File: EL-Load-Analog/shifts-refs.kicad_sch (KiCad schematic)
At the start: 37 parts, among them U10 TL072/OPA2376, U16 TPS7A2030, U17 TPS72325, U21 LT1964-5, U22 AMS1117, U23 TLV1117-50, U4 REF5025AD

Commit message: Working on #4,#2 fixed #8,#22
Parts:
- removed R39: 91, Resistor_SMD:R_0805_2012Metric, symbol Device:R_Small
- C29: Part Name C_2.2uF_10V_X7R_10%_0805 -> C_2.2uF_25V_X7R_10%_0805
- R40: value 1k8 -> 200; Part Name R_1.8kΩ_0805_1% -> R_200.0Ω_0805_1%
- R41: value 220 -> 1k8; Part Name R_220.0Ω_0805_1% -> R_1.8kΩ_0805_1%
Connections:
- net +12V: now also R40.1
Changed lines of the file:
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@@
   (junction (at 73.66 57.15) (diameter 0) (color 0 0 0 0)
   )
+  (junction (at 208.915 35.56) (diameter 0) (color 0 0 0 0)
+  )
   (junction (at 35.56 71.755) (diameter 0) (color 0 0 0 0)
   )
@@
   )
   (junction (at 215.265 81.915) (diameter 0) (color 0 0 0 0)
-  )
-  (junction (at 208.915 35.56) (diameter 0) (color 0 0 0 0)
   )
   (junction (at 82.55 43.18) (diameter 0) (color 0 0 0 0)
@@
     (stroke (width 0) (type default))
   )
+  (wire (pts (xy 208.915 35.56) (xy 215.265 35.56))
+    (stroke (width 0) (type default))
+  )
   (polyline (pts (xy 13.97 114.935) (xy 180.34 114.935))
     (stroke (width 0) (type dash))
@@
     (stroke (width 0) (type default))
   )
-  (wire (pts (xy 208.915 40.64) (xy 208.915 41.91))
+  (wire (pts (xy 208.915 35.56) (xy 208.915 41.91))
     (stroke (width 0) (type default))
   )
@@
     (stroke (width 0) (type default))
   )
+  (wire (pts (xy 255.27 70.485) (xy 255.27 67.945))
+    (stroke (width 0) (type default))
+  )
+  (wire (pts (xy 204.47 54.61) (xy 208.915 54.61))
+    (stroke (width 0) (type default))
+  )
+  (wire (pts (xy 64.77 55.88) (xy 64.77 57.15))
+    (stroke (width 0) (type default))
+  )
+  (wire (pts (xy 109.855 132.715) (xy 109.855 133.985))
+    (stroke (width 0) (type default))
+  )
+  (wire (pts (xy 114.3 48.26) (xy 114.3 54.61))
+    (stroke (width 0) (type default))
+  )
+  (wire (pts (xy 64.77 57.15) (xy 73.66 57.15))
+    (stroke (width 0) (type default))
+  )
+  (wire (pts (xy 106.68 179.705) (xy 109.22 179.705))
+    (stroke (width 0) (type default))
+  )
+  (wire (pts (xy 244.475 67.945) (xy 244.475 70.485))
+    (stroke (width 0) (type default))
+  )
   (wire (pts (xy 208.28 35.56) (xy 208.915 35.56))
-    (stroke (width 0) (type default))
-  )
-  (wire (pts (xy 255.27 70.485) (xy 255.27 67.945))
-    (stroke (width 0) (type default))
-  )
-  (wire (pts (xy 204.47 54.61) (xy 208.915 54.61))
-    (stroke (width 0) (type default))
-  )
-  (wire (pts (xy 64.77 55.88) (xy 64.77 57.15))
-    (stroke (width 0) (type default))
-  )
-  (wire (pts (xy 109.855 132.715) (xy 109.855 133.985))
-    (stroke (width 0) (type default))
-  )
-  (wire (pts (xy 114.3 48.26) (xy 114.3 54.61))
-    (stroke (width 0) (type default))
-  )
-  (wire (pts (xy 64.77 57.15) (xy 73.66 57.15))
-    (stroke (width 0) (type default))
-  )
-  (wire (pts (xy 106.68 179.705) (xy 109.22 179.705))
-    (stroke (width 0) (type default))
-  )
-  (wire (pts (xy 244.475 67.945) (xy 244.475 70.485))
-    (stroke (width 0) (type default))
-  )
-  (wire (pts (xy 208.915 35.56) (xy 215.265 35.56))
     (stroke (width 0) (type default))
   )
@@
       (effects (font (size 1.27 1.27)) hide)
     )
-    (property "Part Name" "C_2.2uF_10V_X7R_10%_0805" (at 113.03 165.1 0)
+    (property "Part Name" "C_2.2uF_25V_X7R_10%_0805" (at 113.03 165.1 0)
       (effects (font (size 1.27 1.27)) hide)
     )
@@
       (effects (font (size 1.27 1.27)) (justify left))
     )
-    (property "Value" "220" (at 211.455 52.0699 0)
+    (property "Value" "1k8" (at 211.455 52.0699 0)
       (effects (font (size 1.27 1.27)) (justify left))
     )
@@
       (effects (font (size 1.27 1.27)) hide)
     )
-    (property "Part Name" "R_220.0Ω_0805_1%" (at 208.915 50.8 0)
+    (property "Part Name" "R_1.8kΩ_0805_1%" (at 208.915 50.8 0)
       (effects (font (size 1.27 1.27)) hide)
     )
@@
       (effects (font (size 1.27 1.27)) (justify left))
     )
-    (property "Value" "1k8" (at 210.82 45.72 0)
+    (property "Value" "200" (at 210.82 45.72 0)
       (effects (font (size 1.27 1.27)) (justify left))
     )
@@
       (effects (font (size 1.27 1.27)) hide)
     )
-    (property "Part Name" "R_1.8kΩ_0805_1%" (at 208.915 44.45 0)
+    (property "Part Name" "R_200.0Ω_0805_1%" (at 208.915 44.45 0)
       (effects (font (size 1.27 1.27)) hide)
     )
@@
     )
   )
-  (symbol (lib_id "Device:R_Small") (at 208.915 38.1 0) (unit 1)
-    (in_bom yes) (on_board yes) (dnp no) (fields_autoplaced)
-    (property "Reference" "R39" (at 210.82 36.83 0)
-      (effects (font (size 1.27 1.27)) (justify left))
-    )
-    (property "Value" "91" (at 210.82 39.37 0)
-      (effects (font (size 1.27 1.27)) (justify left))
-    )
-    (property "Footprint" "Resistor_SMD:R_0805_2012Metric" (at 208.915 38.1 0)
-      (effects (font (size 1.27 1.27)) hide)
-    )
-    (property "Datasheet" "~" (at 208.915 38.1 0)
-      (effects (font (size 1.27 1.27)) hide)
-    )
-    (property "Part Name" "R_91.0Ω_0805_1%" (at 208.915 38.1 0)
-      (effects (font (size 1.27 1.27)) hide)
-    )
-    (pin "1")
-    (pin "2")
-    (instances
-      (project "EL-Load-Analog"
-        (path "/51d9228f-95b8-4f0d-bdba-83c3975c517c/73a2922e-6b99-4e2c-8c0a-1f11161a60e3"
-          (reference "R39") (unit 1)
-        )
-      )
-    )
-  )
   (symbol (lib_id "power:-6V") (at 215.265 88.9 180) (unit 1)
     (in_bom yes) (on_board yes) (dnp no) (fields_autoplaced)
@@
       (effects (font (size 1.27 1.27)) hide)
     )
-    (property "Part Name" "C_2.2uF_10V_X7R_10%_0805" (at 79.375 163.83 0)
-      (effects (font (size 1.27 1.27)) hide)
-    )
+    (property "Part Name" "C_2.2uF_25V_X7R_10%_0805" (at 79.375 163.83 0)
+      (effects (font (size 1.27 1.27)) hide)
+    )

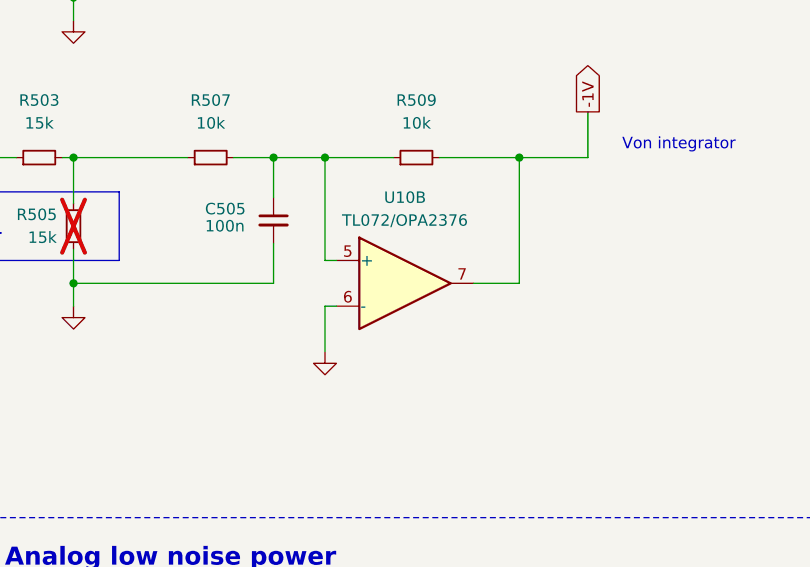
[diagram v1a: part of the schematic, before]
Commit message: Fixing issues from #4, adding ESD protection (#6)
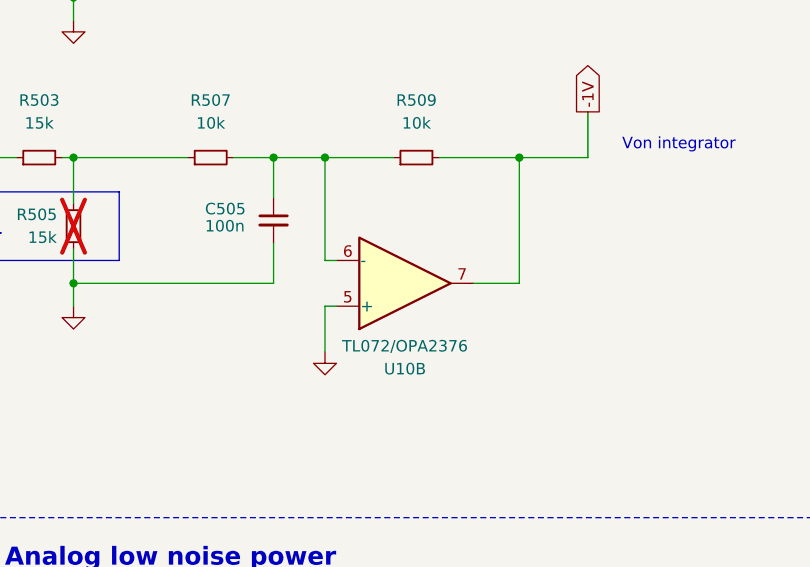
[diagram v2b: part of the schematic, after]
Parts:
- U21: Part Name U_LT1964ES5 -> U_LT1964ES5-5
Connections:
- net GND: now also U10.5 (+); no longer U10.6 (-)
- net at C505.1, R507.2, R509.1: now also U10.6 (-); no longer U10.5 (+)
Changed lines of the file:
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@@
       (effects (font (size 1.27 1.27)) hide)
     )
-    (property "Part Name" "U_LT1964ES5" (at 230.505 79.375 0)
+    (property "Part Name" "U_LT1964ES5-5" (at 230.505 79.375 0)
       (effects (font (size 1.27 1.27)) hide)
     )
@@
     )
   )
-  (symbol (lib_id "Amplifier_Operational:TL072") (at 128.27 88.9 0) (unit 2)
-    (in_bom yes) (on_board yes) (dnp no) (fields_autoplaced)
-    (property "Reference" "U10" (at 128.27 79.375 0)
+  (symbol (lib_id "Amplifier_Operational:TL072") (at 128.27 88.9 0) (mirror x) (unit 2)
+    (in_bom yes) (on_board yes) (dnp no)
+    (property "Reference" "U10" (at 128.27 98.425 0)
       (effects (font (size 1.27 1.27)))
     )
-    (property "Value" "TL072/OPA2376" (at 128.27 81.915 0)
+    (property "Value" "TL072/OPA2376" (at 128.27 95.885 0)
       (effects (font (size 1.27 1.27)))
     )

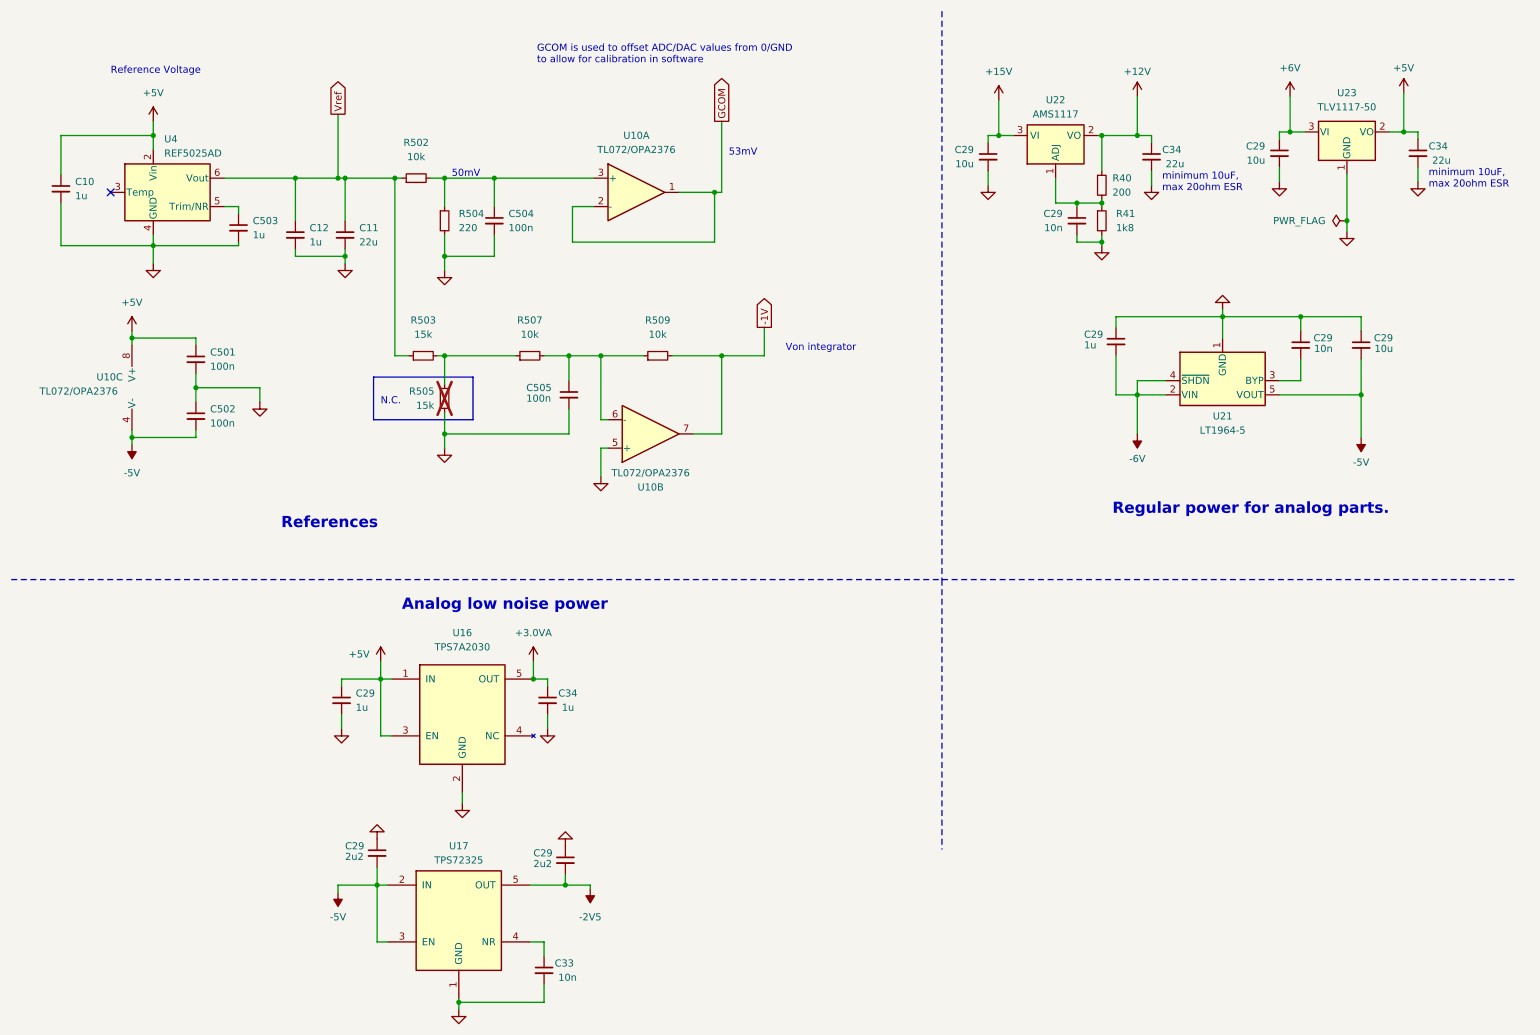
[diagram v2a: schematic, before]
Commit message: Added heatsink moutingholes, reverse polarity, moved snubbers.
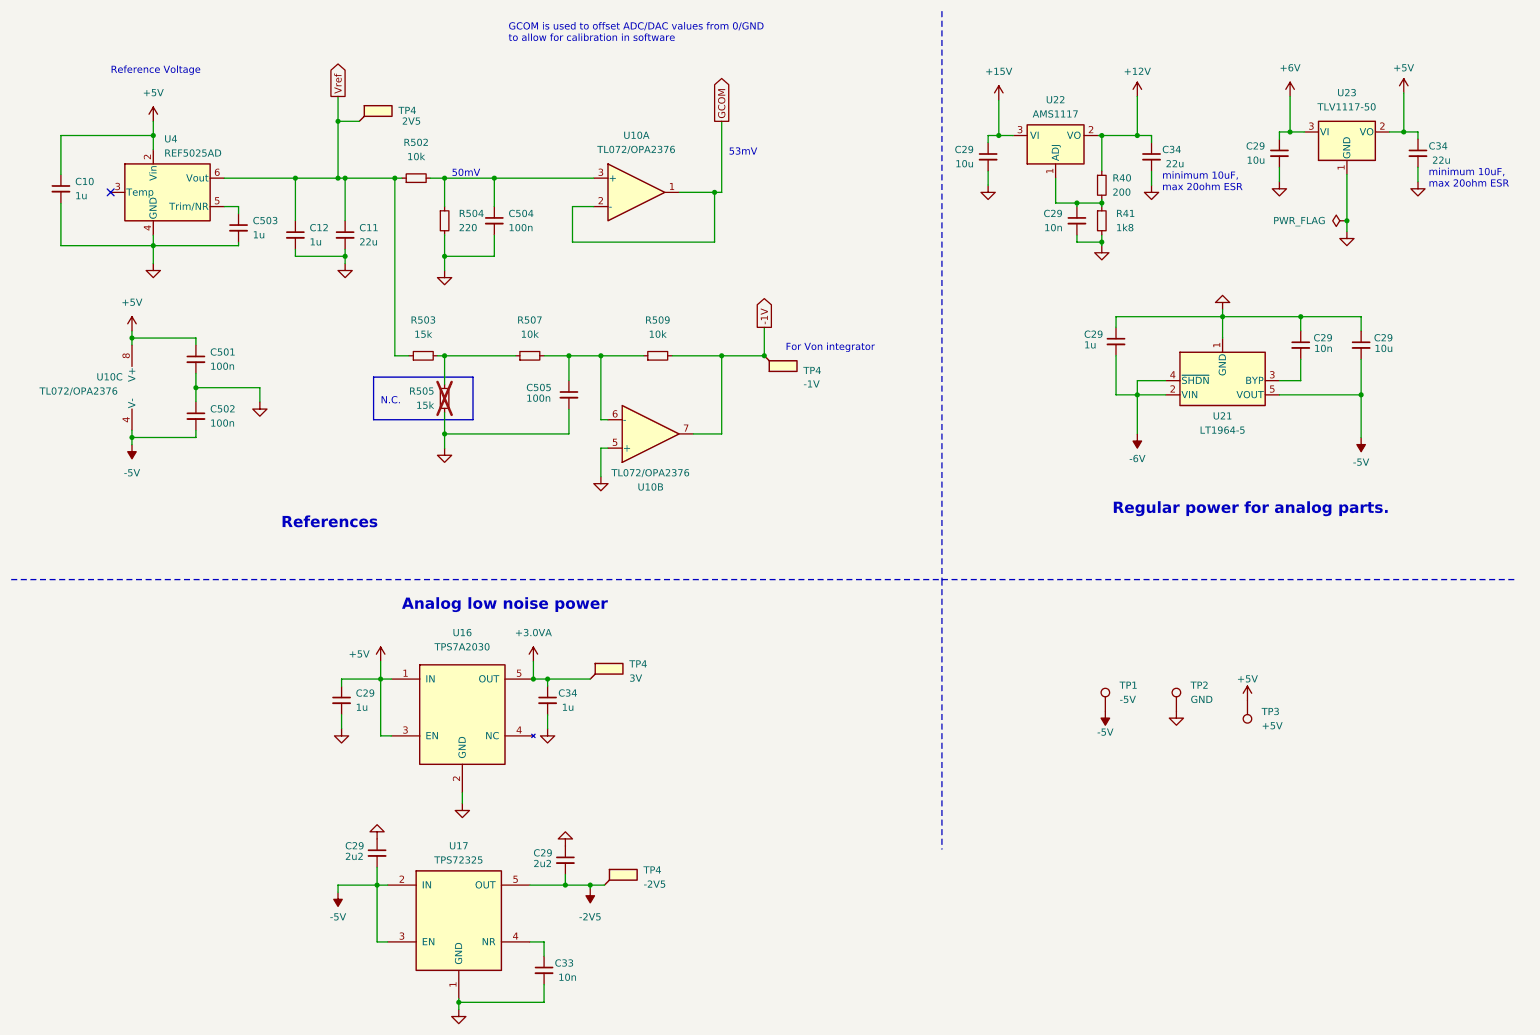
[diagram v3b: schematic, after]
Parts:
- added TP1: -5V, TestPoint:TestPoint_Loop_D1.80mm_Drill1.0mm_Beaded, symbol Connector:TestPoint
- added TP2: GND, TestPoint:TestPoint_Loop_D2.50mm_Drill1.0mm, symbol Connector:TestPoint
- added TP3: +5V, TestPoint:TestPoint_Loop_D1.80mm_Drill1.0mm_Beaded, symbol Connector:TestPoint
- added TP4: 3V, TestPoint:TestPoint_Pad_1.0x1.0mm, symbol Connector:TestPoint_Flag
- added TP4: -2V5, TestPoint:TestPoint_Pad_1.0x1.0mm, symbol Connector:TestPoint_Flag
- added TP4: 2V5, TestPoint:TestPoint_Pad_1.0x1.0mm, symbol Connector:TestPoint_Flag
- added TP4: -1V, TestPoint:TestPoint_Pad_1.0x1.0mm, symbol Connector:TestPoint_Flag
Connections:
- net +3.0VA: now also TP4.1
- net +5V: now also TP3.1
- net -1V: now also TP4.1
- net -2V5: now also TP4.1
- net -5V: now also TP1.1
- net GND: now also TP2.1
- net Vref: now also TP4.1
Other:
- note added: "For Von integrator"
- note removed: "Von integrator"

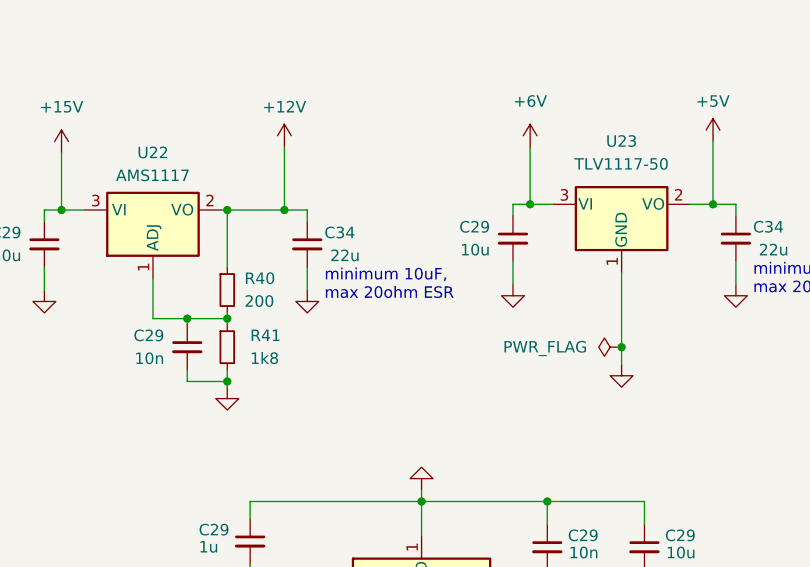
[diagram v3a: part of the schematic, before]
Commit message: v4 Analog board design. Features reverse polarity, remote sense error and new clamping circuitry.
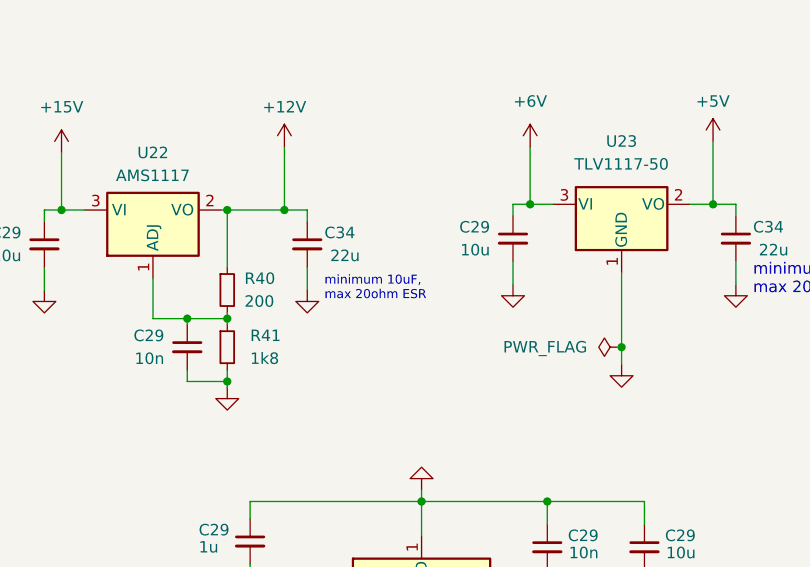
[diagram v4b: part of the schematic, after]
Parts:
- C29: Part Name C_10.0uF_25V_X7R_10%_0805 -> C_10.0uF_25V_X5R_10%_0805
- C501, C502, C504, C505: Part Name C_100.0nF_0805_20% -> C_100.0nF_50V_0805_10%_X7R
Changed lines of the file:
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@@
   (title_block
     (title "Electronic Load Analog Test Board")
-    (date "2024-02-06")
+    (date "2024-11-10")
     (rev "${VERSION}")
     (comment 1 "License: CERN-OHL-W-2.0")
@@
   )
   (text "minimum 10uF, \nmax 20ohm ESR" (at 219.71 45.72 0)
-    (effects (font (size 1.27 1.27)) (justify left bottom))
+    (effects (font (size 1 1)) (justify left bottom))
   )
   (text "GCOM is used to offset ADC/DAC values from 0/GND \nto allow for calibration in software\n"
@@
       (effects (font (size 1.27 1.27)) hide)
     )
-    (property "Part Name" "C_10.0uF_25V_X7R_10%_0805" (at 255.27 73.025 0)
+    (property "Part Name" "C_10.0uF_25V_X5R_10%_0805" (at 255.27 73.025 0)
       (effects (font (size 1.27 1.27)) hide)
     )
@@
       (effects (font (size 1.27 1.27)) hide)
     )
-    (property "Part Name" "C_10.0uF_25V_X7R_10%_0805" (at 240.665 38.735 0)
+    (property "Part Name" "C_10.0uF_25V_X5R_10%_0805" (at 240.665 38.735 0)
       (effects (font (size 1.27 1.27)) hide)
     )
@@
       (effects (font (size 1.27 1.27)) hide)
     )
-    (property "Part Name" "C_100.0nF_0805_20%" (at 46.99 75.565 0)
+    (property "Part Name" "C_100.0nF_50V_0805_10%_X7R " (at 46.99 75.565 0)
       (effects (font (size 1.27 1.27)) hide)
     )
@@
       (effects (font (size 1.27 1.27)) hide)
     )
-    (property "Part Name" "C_10.0uF_25V_X7R_10%_0805" (at 188.595 39.37 0)
+    (property "Part Name" "C_10.0uF_25V_X5R_10%_0805" (at 188.595 39.37 0)
       (effects (font (size 1.27 1.27)) hide)
     )
@@
       (effects (font (size 1.27 1.27)) hide)
     )
-    (property "Part Name" "C_100.0nF_0805_20%" (at 100.33 50.8 0)
+    (property "Part Name" "C_100.0nF_50V_0805_10%_X7R " (at 100.33 50.8 0)
       (effects (font (size 1.27 1.27)) hide)
     )
@@
       (effects (font (size 1.27 1.27)) hide)
     )
-    (property "Part Name" "C_100.0nF_0805_20%" (at 113.665 81.915 0)
+    (property "Part Name" "C_100.0nF_50V_0805_10%_X7R " (at 113.665 81.915 0)
       (effects (font (size 1.27 1.27)) hide)
     )
@@
       (effects (font (size 1.27 1.27)) hide)
     )
-    (property "Part Name" "C_100.0nF_0805_20%" (at 46.99 85.725 0)
-      (effects (font (size 1.27 1.27)) hide)
-    )
+    (property "Part Name" "C_100.0nF_50V_0805_10%_X7R " (at 46.99 85.725 0)
+      (effects (font (size 1.27 1.27)) hide)
+    )
